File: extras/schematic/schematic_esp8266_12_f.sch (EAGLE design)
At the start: 26 parts, among them U1 SI4735-D60-GU

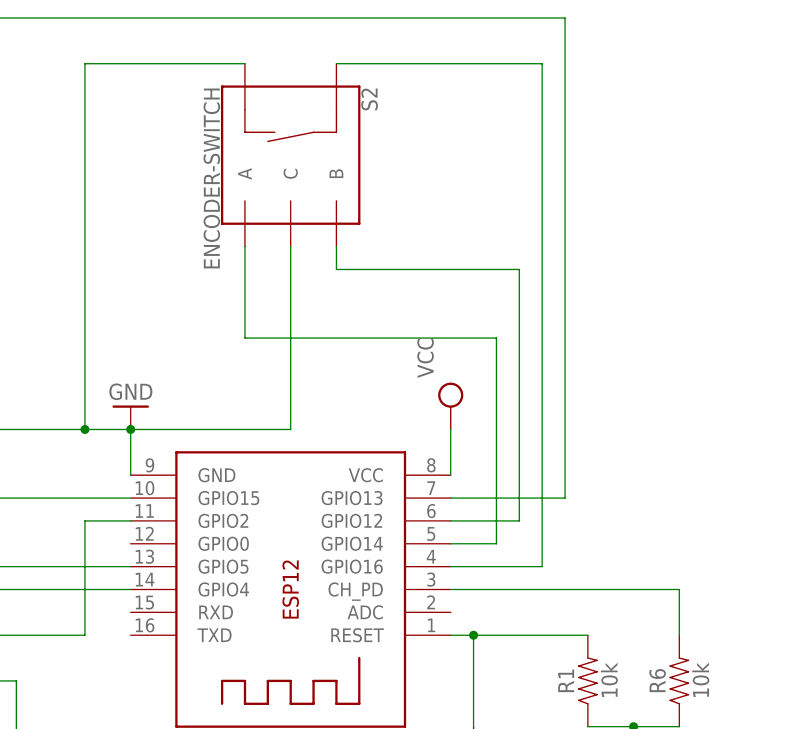
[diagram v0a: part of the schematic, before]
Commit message: SI473X Arduino Library
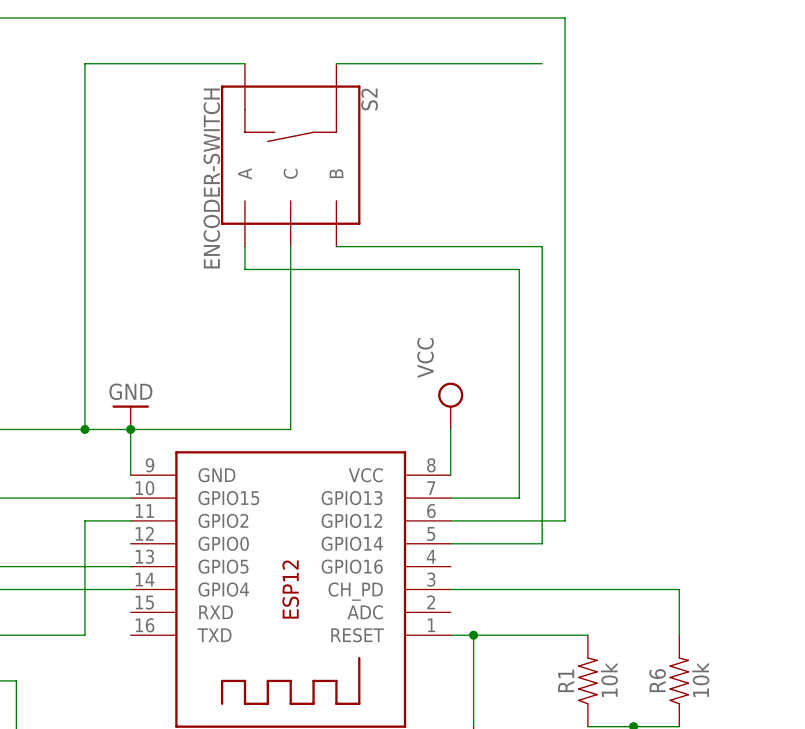
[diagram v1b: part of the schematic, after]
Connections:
- net N$17: now also X1.GPIO14; no longer X1.GPIO12
- net N$18: now also X1.GPIO13; no longer X1.GPIO14
- net N$20: no longer X1.GPIO16
- net N$21: now also X1.GPIO12; no longer X1.GPIO13
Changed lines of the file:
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@@
-</segment>
-</net>
-<net name="N$17" class="0">
-<segment>
-<pinref part="S2" gate="G$1" pin="B"/>
-<wire x1="106.68" y1="132.08" x2="106.68" y2="129.54" width="0.1524" layer="91"/>
-<wire x1="106.68" y1="129.54" x2="127" y2="129.54" width="0.1524" layer="91"/>
-<pinref part="X1" gate="G$1" pin="GPIO12"/>
-<wire x1="127" y1="129.54" x2="127" y2="101.6" width="0.1524" layer="91"/>
-<wire x1="127" y1="101.6" x2="119.38" y2="101.6" width="0.1524" layer="91"/>
-</segment>
-</net>
-<net name="N$18" class="0">
-<segment>
-<pinref part="S2" gate="G$1" pin="A"/>
-<wire x1="96.52" y1="132.08" x2="96.52" y2="121.92" width="0.1524" layer="91"/>
-<wire x1="96.52" y1="121.92" x2="124.46" y2="121.92" width="0.1524" layer="91"/>
-<wire x1="124.46" y1="121.92" x2="124.46" y2="99.06" width="0.1524" layer="91"/>
-<pinref part="X1" gate="G$1" pin="GPIO14"/>
-<wire x1="124.46" y1="99.06" x2="119.38" y2="99.06" width="0.1524" layer="91"/>
 </segment>
 </net>
@@
 <pinref part="S2" gate="G$1" pin="SW+"/>
 <wire x1="106.68" y1="152.4" x2="129.54" y2="152.4" width="0.1524" layer="91"/>
-<wire x1="129.54" y1="152.4" x2="129.54" y2="96.52" width="0.1524" layer="91"/>
-<pinref part="X1" gate="G$1" pin="GPIO16"/>
-<wire x1="129.54" y1="96.52" x2="119.38" y2="96.52" width="0.1524" layer="91"/>
 </segment>
 </net>
@@
 <wire x1="68.58" y1="132.08" x2="68.58" y2="157.48" width="0.1524" layer="91"/>
 <wire x1="68.58" y1="157.48" x2="132.08" y2="157.48" width="0.1524" layer="91"/>
-<wire x1="132.08" y1="157.48" x2="132.08" y2="104.14" width="0.1524" layer="91"/>
-<pinref part="X1" gate="G$1" pin="GPIO13"/>
-<wire x1="132.08" y1="104.14" x2="119.38" y2="104.14" width="0.1524" layer="91"/>
+<wire x1="132.08" y1="157.48" x2="132.08" y2="101.6" width="0.1524" layer="91"/>
+<pinref part="X1" gate="G$1" pin="GPIO12"/>
+<wire x1="119.38" y1="101.6" x2="132.08" y2="101.6" width="0.1524" layer="91"/>
 </segment>
 </net>
@@
 </segment>
 </net>
+<net name="N$17" class="0">
+<segment>
+<pinref part="X1" gate="G$1" pin="GPIO14"/>
+<wire x1="119.38" y1="99.06" x2="129.54" y2="99.06" width="0.1524" layer="91"/>
+<wire x1="129.54" y1="99.06" x2="129.54" y2="132.08" width="0.1524" layer="91"/>
+<pinref part="S2" gate="G$1" pin="B"/>
+<wire x1="129.54" y1="132.08" x2="106.68" y2="132.08" width="0.1524" layer="91"/>
+</segment>
+</net>
+<net name="N$18" class="0">
+<segment>
+<pinref part="X1" gate="G$1" pin="GPIO13"/>
+<wire x1="119.38" y1="104.14" x2="127" y2="104.14" width="0.1524" layer="91"/>
+<wire x1="127" y1="104.14" x2="127" y2="129.54" width="0.1524" layer="91"/>
+<wire x1="127" y1="129.54" x2="96.52" y2="129.54" width="0.1524" layer="91"/>
+<pinref part="S2" gate="G$1" pin="A"/>
+<wire x1="96.52" y1="129.54" x2="96.52" y2="132.08" width="0.1524" layer="91"/>
+</segment>
+</net>

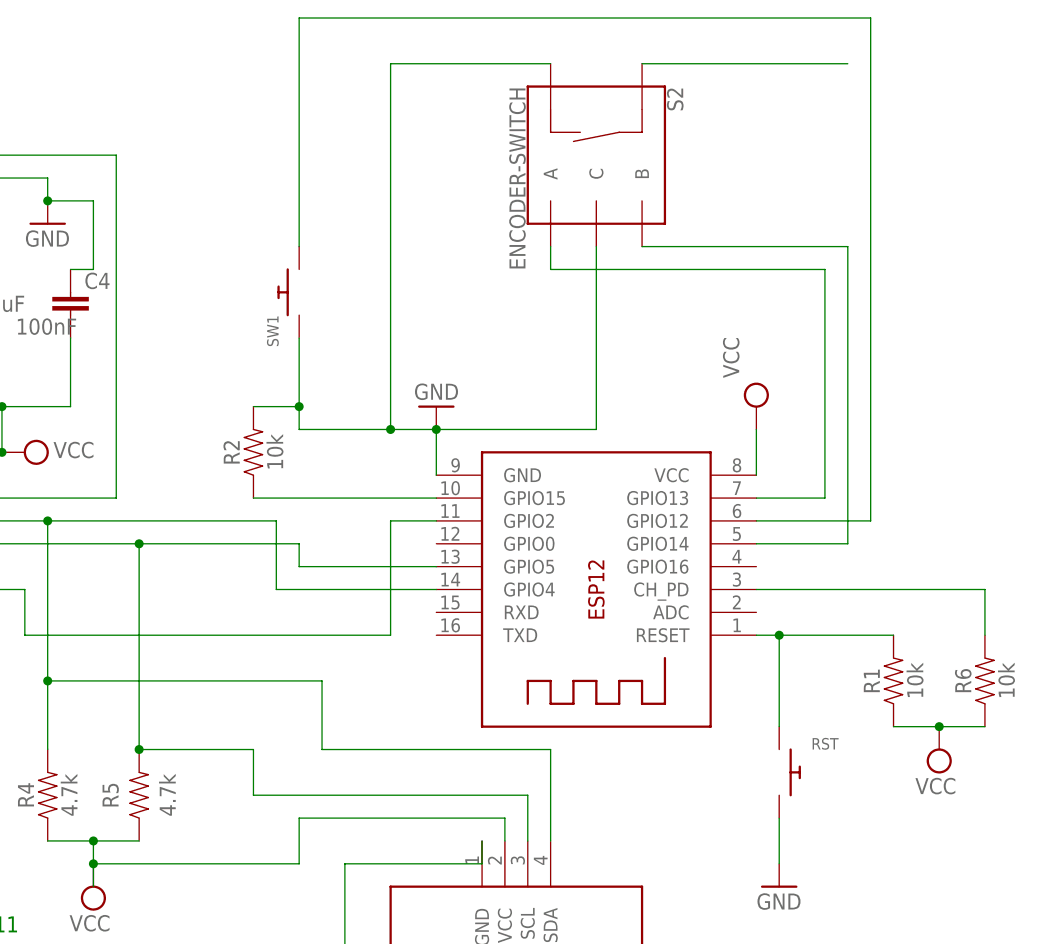
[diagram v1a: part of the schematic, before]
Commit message: SI473X Arduino Library
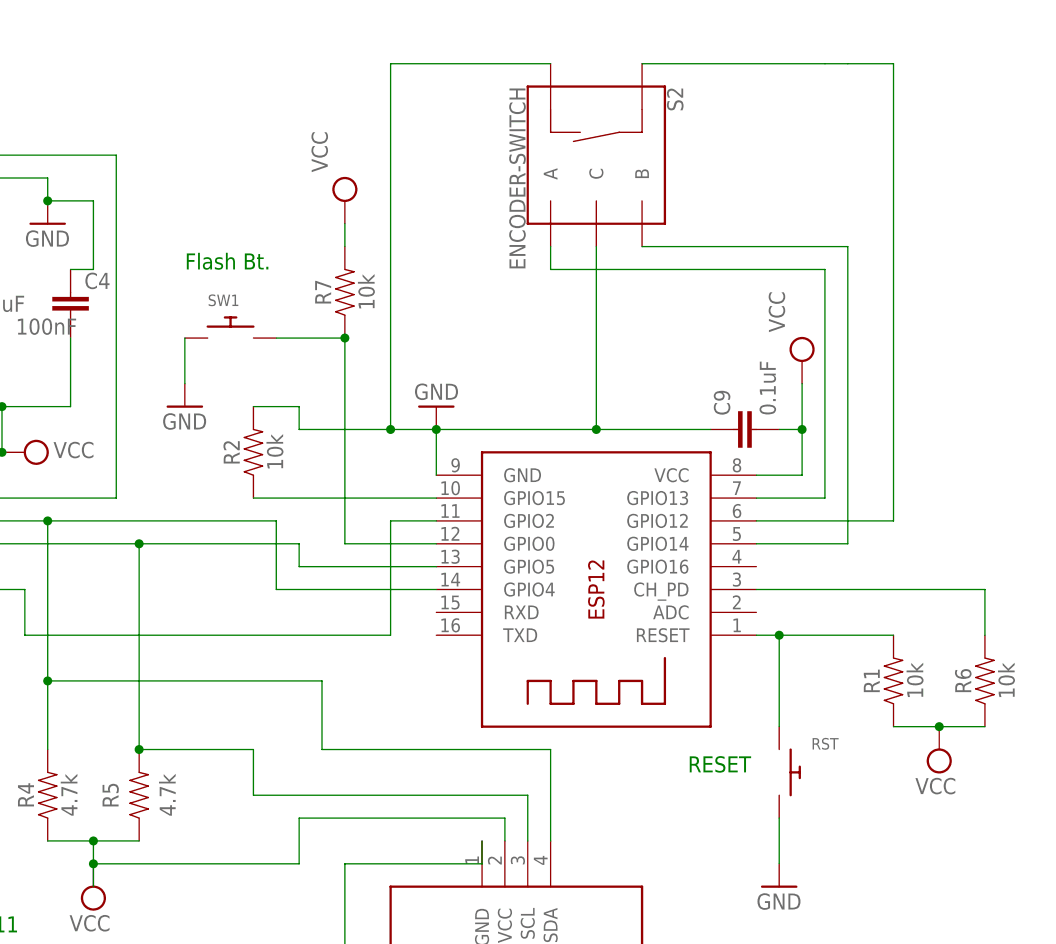
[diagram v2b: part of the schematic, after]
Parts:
- added C9: 0.1uF, SparkFun-Capacitors:0.1UF-0402-16V-10%
- added R7: 10k, SparkFun-Resistors:10KOHM-0603-1/10W-1%
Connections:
- removed net N$21: SW1.P$2, X1.GPIO12
- new net N$24: S2.SW+, X1.GPIO12
- net GND: now also C9.1
- net N$20: now also R7.1, SW1.P$2, X1.GPIO0; no longer S2.SW+
- net VCC: now also C9.2, R7.2
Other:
- note added: "Flash Bt."
- note added: "RESET"
- moved on the sheet: SW1
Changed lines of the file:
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@@
 <layers>
 <layer number="1" name="Top" color="4" fill="1" visible="no" active="no"/>
+<layer number="2" name="Route2" color="1" fill="3" visible="no" active="no"/>
+<layer number="3" name="Route3" color="4" fill="3" visible="no" active="no"/>
+<layer number="4" name="Route4" color="1" fill="4" visible="no" active="no"/>
+<layer number="5" name="Route5" color="4" fill="4" visible="no" active="no"/>
+<layer number="6" name="Route6" color="1" fill="8" visible="no" active="no"/>
+<layer number="7" name="Route7" color="4" fill="8" visible="no" active="no"/>
+<layer number="8" name="Route8" color="1" fill="2" visible="no" active="no"/>
+<layer number="9" name="Route9" color="4" fill="2" visible="no" active="no"/>
+<layer number="10" name="Route10" color="1" fill="7" visible="no" active="no"/>
+<layer number="11" name="Route11" color="4" fill="7" visible="no" active="no"/>
+<layer number="12" name="Route12" color="1" fill="5" visible="no" active="no"/>
+<layer number="13" name="Route13" color="4" fill="5" visible="no" active="no"/>
+<layer number="14" name="Route14" color="1" fill="6" visible="no" active="no"/>
+<layer number="15" name="Route15" color="4" fill="6" visible="no" active="no"/>
 <layer number="16" name="Bottom" color="1" fill="1" visible="no" active="no"/>
 <layer number="17" name="Pads" color="2" fill="1" visible="no" active="no"/>
@@
 <part name="U$1" library="diy-modules" deviceset="DISPLAY-OLED-128X64-I2C" device=""/>
 <part name="GND2" library="supply1" library_urn="urn:adsk.eagle:library:371" deviceset="GND" device=""/>
-<part name="SW1" library="adafruit" library_urn="urn:adsk.eagle:library:420" deviceset="SWITCH_PUSHBUTTON" device="C&amp;K_KSS" package3d_urn="urn:adsk.eagle:package:6240958/1"/>
 <part name="R1" library="SparkFun-Resistors" library_urn="urn:adsk.eagle:library:532" deviceset="10KOHM" device="-0603-1/10W-1%" package3d_urn="urn:adsk.eagle:package:39650/1" value="10k"/>
 <part name="R2" library="SparkFun-Resistors" library_urn="urn:adsk.eagle:library:532" deviceset="10KOHM" device="-0603-1/10W-1%" package3d_urn="urn:adsk.eagle:package:39650/1" value="10k"/>
@@
 <part name="RST" library="adafruit" library_urn="urn:adsk.eagle:library:420" deviceset="SWITCH_PUSHBUTTON" device="C&amp;K_KSS" package3d_urn="urn:adsk.eagle:package:6240958/1"/>
 <part name="GND8" library="supply1" library_urn="urn:adsk.eagle:library:371" deviceset="GND" device=""/>
+<part name="C9" library="SparkFun-Capacitors" library_urn="urn:adsk.eagle:library:510" deviceset="0.1UF" device="-0402-16V-10%" package3d_urn="urn:adsk.eagle:package:37413/1" value="0.1uF"/>
+<part name="SUPPLY6" library="supply2" library_urn="urn:adsk.eagle:library:372" deviceset="VCC" device=""/>
+<part name="R7" library="SparkFun-Resistors" library_urn="urn:adsk.eagle:library:532" deviceset="10KOHM" device="-0603-1/10W-1%" package3d_urn="urn:adsk.eagle:package:39650/1" value="10k"/>
+<part name="SW1" library="adafruit" library_urn="urn:adsk.eagle:library:420" deviceset="SWITCH_PUSHBUTTON" device="C&amp;K_KSS" package3d_urn="urn:adsk.eagle:package:6240958/1"/>
+<part name="GND9" library="supply1" library_urn="urn:adsk.eagle:library:371" deviceset="GND" device=""/>
 </parts>
 <sheets>
@@
     TX  &lt;-&gt; RX
 GPIO0 &lt;-&gt; DTS</text>
+<text x="55.88" y="129.54" size="1.778" layer="91">Flash Bt.</text>
+<text x="111.76" y="73.66" size="1.778" layer="91">RESET</text>
 </plain>
 <instances>
@@
 <attribute name="VALUE" x="86.36" y="116.84" size="1.778" layer="96" rot="R180"/>
 </instance>
-<instance part="SUPPLY2" gate="G$1" x="119.38" y="114.3" smashed="yes">
-<attribute name="VALUE" x="117.475" y="117.475" size="1.778" layer="96" rot="R90"/>
+<instance part="SUPPLY2" gate="G$1" x="124.46" y="119.38" smashed="yes">
+<attribute name="VALUE" x="122.555" y="122.555" size="1.778" layer="96" rot="R90"/>
 </instance>
 <instance part="GND7" gate="1" x="-71.12" y="86.36" smashed="yes">
@@
 <attribute name="VALUE" x="71.12" y="43.18" size="1.778" layer="96"/>
 </instance>
-<instance part="SW1" gate="G$1" x="68.58" y="127" smashed="yes" rot="R90">
-<attribute name="NAME" x="65.024" y="124.46" size="1.27" layer="95" rot="R270"/>
-<attribute name="VALUE" x="70.866" y="124.46" size="1.27" layer="96" rot="R270"/>
-</instance>
 <instance part="R1" gate="G$1" x="134.62" y="83.82" smashed="yes" rot="R90">
 <attribute name="NAME" x="133.096" y="83.82" size="1.778" layer="95" font="vector" rot="R90" align="bottom-center"/>
@@
 <instance part="GND8" gate="1" x="121.92" y="60.96" smashed="yes">
 <attribute name="VALUE" x="119.38" y="58.42" size="1.778" layer="96"/>
+</instance>
+<instance part="C9" gate="G$1" x="119.38" y="111.76" smashed="yes" rot="R90">
+<attribute name="NAME" x="116.459" y="113.284" size="1.778" layer="95" font="vector" rot="R90"/>
+<attribute name="VALUE" x="121.539" y="113.284" size="1.778" layer="96" font="vector" rot="R90"/>
+</instance>
+<instance part="SUPPLY6" gate="G$1" x="73.66" y="137.16" smashed="yes">
+<attribute name="VALUE" x="71.755" y="140.335" size="1.778" layer="96" rot="R90"/>
+</instance>
+<instance part="R7" gate="G$1" x="73.66" y="127" smashed="yes" rot="R90">
+<attribute name="NAME" x="72.136" y="127" size="1.778" layer="95" font="vector" rot="R90" align="bottom-center"/>
+<attribute name="VALUE" x="75.184" y="127" size="1.778" layer="96" font="vector" rot="R90" align="top-center"/>
+</instance>
+<instance part="SW1" gate="G$1" x="60.96" y="121.92" smashed="yes">
+<attribute name="NAME" x="58.42" y="125.476" size="1.27" layer="95"/>
+<attribute name="VALUE" x="58.42" y="119.634" size="1.27" layer="96"/>
+</instance>
+<instance part="GND9" gate="1" x="55.88" y="114.3" smashed="yes">
+<attribute name="VALUE" x="53.34" y="111.76" size="1.778" layer="96"/>
 </instance>
 </instances>
@@
 <wire x1="101.6" y1="132.08" x2="101.6" y2="111.76" width="0.1524" layer="91"/>
 <wire x1="101.6" y1="111.76" x2="83.82" y2="111.76" width="0.1524" layer="91"/>
-<pinref part="SW1" gate="G$1" pin="P$1"/>
-<wire x1="68.58" y1="121.92" x2="68.58" y2="114.3" width="0.1524" layer="91"/>
 <wire x1="68.58" y1="114.3" x2="68.58" y2="111.76" width="0.1524" layer="91"/>
 <wire x1="68.58" y1="111.76" x2="78.74" y2="111.76" width="0.1524" layer="91"/>
@@
 <pinref part="R2" gate="G$1" pin="2"/>
 <wire x1="63.5" y1="114.3" x2="68.58" y2="114.3" width="0.1524" layer="91"/>
-<junction x="68.58" y="114.3"/>
+<pinref part="C9" gate="G$1" pin="1"/>
+<wire x1="114.3" y1="111.76" x2="101.6" y2="111.76" width="0.1524" layer="91"/>
+<junction x="101.6" y="111.76"/>
 </segment>
 <segment>
@@
 <pinref part="RST" gate="G$1" pin="P$2"/>
 <wire x1="121.92" y1="63.5" x2="121.92" y2="68.58" width="0.1524" layer="91"/>
+</segment>
+<segment>
+<pinref part="SW1" gate="G$1" pin="P$1"/>
+<pinref part="GND9" gate="1" pin="GND"/>
+<wire x1="55.88" y1="121.92" x2="55.88" y2="116.84" width="0.1524" layer="91"/>
 </segment>
 </net>
@@
 </segment>
 <segment>
-<pinref part="X1" gate="G$1" pin="VCC"/>
-<pinref part="SUPPLY2" gate="G$1" pin="VCC"/>
-<wire x1="119.38" y1="106.68" x2="119.38" y2="111.76" width="0.1524" layer="91"/>
-</segment>
-<segment>
 <pinref part="R1" gate="G$1" pin="1"/>
 <pinref part="R6" gate="G$1" pin="1"/>
@@
 <wire x1="139.7" y1="78.74" x2="144.78" y2="78.74" width="0.1524" layer="91"/>
 <junction x="139.7" y="78.74"/>
+</segment>
+<segment>
+<pinref part="SUPPLY2" gate="G$1" pin="VCC"/>
+<wire x1="124.46" y1="116.84" x2="124.46" y2="111.76" width="0.1524" layer="91"/>
+<pinref part="X1" gate="G$1" pin="VCC"/>
+<wire x1="124.46" y1="111.76" x2="124.46" y2="106.68" width="0.1524" layer="91"/>
+<wire x1="124.46" y1="106.68" x2="119.38" y2="106.68" width="0.1524" layer="91"/>
+<pinref part="C9" gate="G$1" pin="2"/>
+<wire x1="121.92" y1="111.76" x2="124.46" y2="111.76" width="0.1524" layer="91"/>
+<junction x="124.46" y="111.76"/>
+</segment>
+<segment>
+<pinref part="SUPPLY6" gate="G$1" pin="VCC"/>
+<pinref part="R7" gate="G$1" pin="2"/>
+<wire x1="73.66" y1="134.62" x2="73.66" y2="132.08" width="0.1524" layer="91"/>
 </segment>
 </net>
@@
 </segment>
 </net>
-<net name="N$20" class="0">
-<segment>
-<pinref part="S2" gate="G$1" pin="SW+"/>
-<wire x1="106.68" y1="152.4" x2="129.54" y2="152.4" width="0.1524" layer="91"/>
-</segment>
-</net>
-<net name="N$21" class="0">
-<segment>
-<pinref part="SW1" gate="G$1" pin="P$2"/>
-<wire x1="68.58" y1="132.08" x2="68.58" y2="157.48" width="0.1524" layer="91"/>
-<wire x1="68.58" y1="157.48" x2="132.08" y2="157.48" width="0.1524" layer="91"/>
-<wire x1="132.08" y1="157.48" x2="132.08" y2="101.6" width="0.1524" layer="91"/>
-<pinref part="X1" gate="G$1" pin="GPIO12"/>
-<wire x1="119.38" y1="101.6" x2="132.08" y2="101.6" width="0.1524" layer="91"/>
-</segment>
-</net>
 <net name="N$19" class="0">
 <segment>
@@
 </segment>
 </net>
+<net name="N$24" class="0">
+<segment>
+<pinref part="X1" gate="G$1" pin="GPIO12"/>
+<wire x1="119.38" y1="101.6" x2="134.62" y2="101.6" width="0.1524" layer="91"/>
+<wire x1="134.62" y1="101.6" x2="134.62" y2="152.4" width="0.1524" layer="91"/>
+<pinref part="S2" gate="G$1" pin="SW+"/>
+<wire x1="106.68" y1="152.4" x2="127" y2="152.4" width="0.1524" layer="91"/>
+<wire x1="127" y1="152.4" x2="129.54" y2="152.4" width="0.1524" layer="91"/>
+<wire x1="134.62" y1="152.4" x2="129.54" y2="152.4" width="0.1524" layer="91"/>
+</segment>
+</net>
+<net name="N$20" class="0">
+<segment>
+<pinref part="X1" gate="G$1" pin="GPIO0"/>
+<wire x1="83.82" y1="99.06" x2="73.66" y2="99.06" width="0.1524" layer="91"/>
+<pinref part="R7" gate="G$1" pin="1"/>
+<wire x1="73.66" y1="121.92" x2="73.66" y2="99.06" width="0.1524" layer="91"/>
+<pinref part="SW1" gate="G$1" pin="P$2"/>
+<wire x1="66.04" y1="121.92" x2="73.66" y2="121.92" width="0.1524" layer="91"/>
+<junction x="73.66" y="121.92"/>
+</segment>
+</net>
